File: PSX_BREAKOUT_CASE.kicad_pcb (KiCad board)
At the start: 2 copper layers, 100 x 71.1 mm, 11 parts

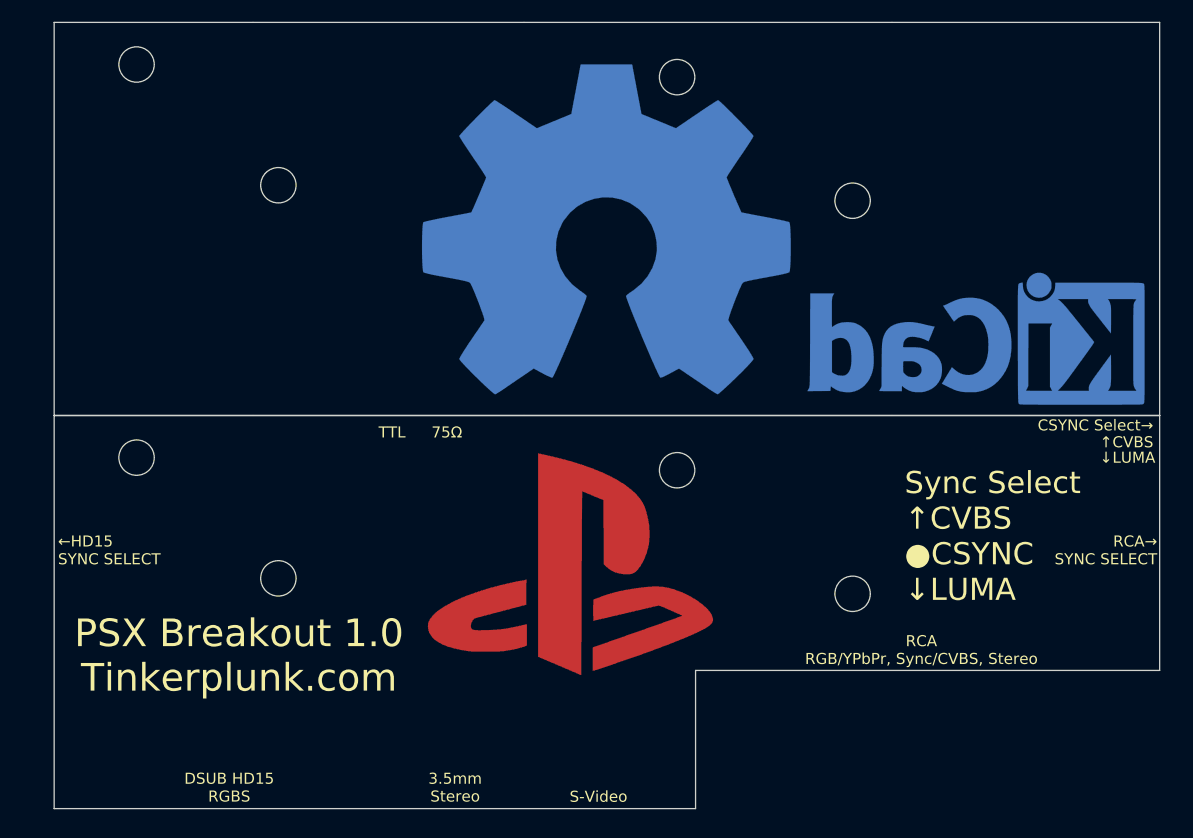
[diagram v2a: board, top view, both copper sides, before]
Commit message: Fixed s-video and headphone footprint, added support hole
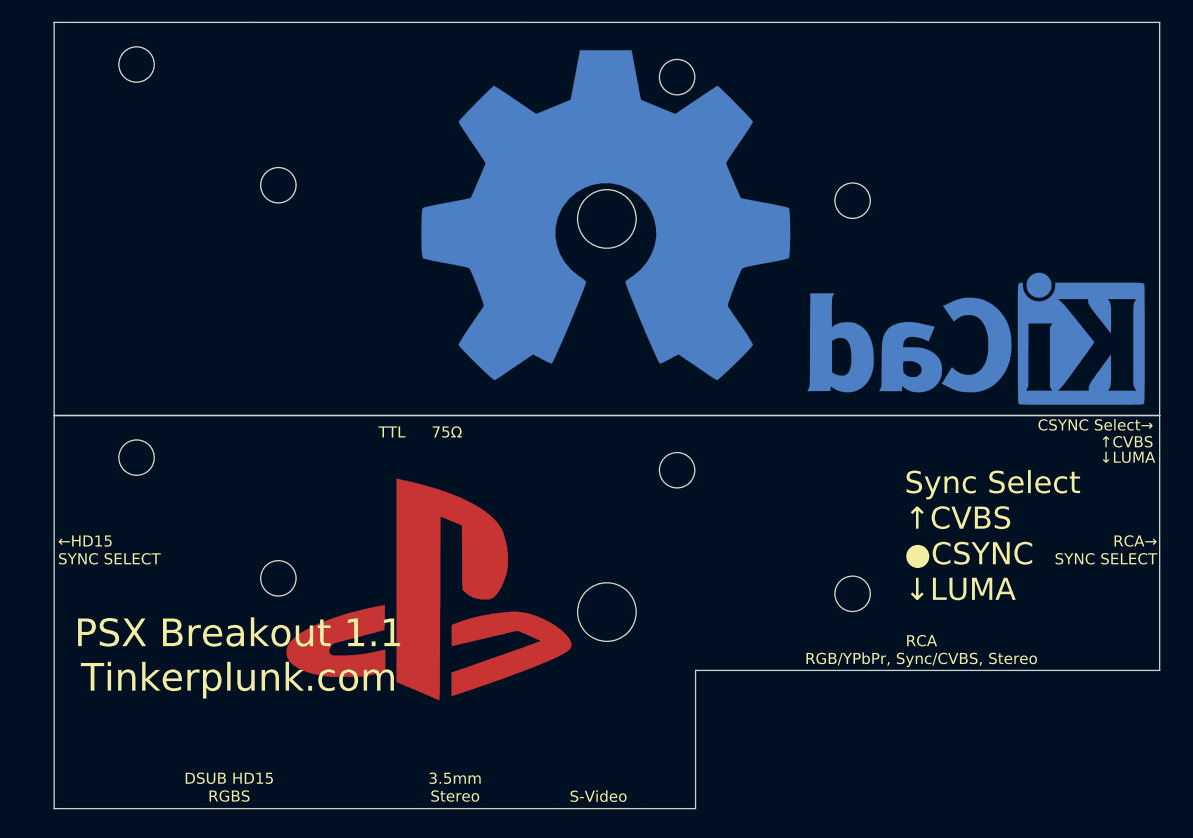
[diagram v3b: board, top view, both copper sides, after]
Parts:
- added REF**: MountingHole_5.3mm_M5, MountingHole:MountingHole_5.3mm_M5, F.Cu at (139.9, 58.4)
- added REF**: MountingHole_5.3mm_M5, MountingHole:MountingHole_5.3mm_M5, F.Cu at (140.0, 94.0)
- moved G*** 13.0 mm to (123.8, 92.0)
- moved REF** 1.29 mm to (139.9, 58.1)
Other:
- board text added: "PSX Breakout 1.1 Tinkerplunk.com"
- board text removed: "PSX Breakout 1.0 Tinkerplunk.com"
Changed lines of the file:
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@@
     (tracks 0)
     (zones 0)
-    (modules 11)
+    (modules 13)
     (nets 1)
   )
@@
     (uvia_drill 0.1)
   )
+  (module MountingHole:MountingHole_5.3mm_M5 (layer F.Cu)
+    (at 139.95 58.42)
+    (descr "Mounting Hole 5.3mm, no annular, M5")
+    (tags "mounting hole 5.3mm no annular m5")
+    (attr virtual)
+    (fp_text reference REF** (at 0 -6.3) (layer F.SilkS) hide
+      (effects (font (size 1 1) (thickness 0.15)))
+    )
+    (fp_text value MountingHole_5.3mm_M5 (at 0 6.3) (layer F.Fab)
+      (effects (font (size 1 1) (thickness 0.15)))
+    )
+    (fp_text user %R (at 0.3 0) (layer F.Fab)
+      (effects (font (size 1 1) (thickness 0.15)))
+    )
+    (fp_circle (center 0 0) (end 2.648001 0) (layer Cmts.User) (width 0.15))
+    (fp_circle (center 0 0) (end 2.648001 0) (layer F.CrtYd) (width 0.05))
+    (pad 1 np_thru_hole circle (at 0 0) (size 5.3 5.3) (drill 5.3) (layers *.Cu *.Mask))
+  )
+  (module MountingHole:MountingHole_5.3mm_M5 (layer F.Cu)
+    (at 139.954 93.98)
+    (descr "Mounting Hole 5.3mm, no annular, M5")
+    (tags "mounting hole 5.3mm no annular m5")
+    (attr virtual)
+    (fp_text reference REF** (at 0 -6.3) (layer F.SilkS) hide
+      (effects (font (size 1 1) (thickness 0.15)))
+    )
+    (fp_text value MountingHole_5.3mm_M5 (at 0 6.3) (layer F.Fab)
+      (effects (font (size 1 1) (thickness 0.15)))
+    )
+    (fp_circle (center 0 0) (end 2.648001 0) (layer F.CrtYd) (width 0.05))
+    (fp_circle (center 0 0) (end 2.648001 0) (layer Cmts.User) (width 0.15))
+    (fp_text user %R (at 0.3 0) (layer F.Fab)
+      (effects (font (size 1 1) (thickness 0.15)))
+    )
+    (pad 1 np_thru_hole circle (at 0 0) (size 5.3 5.3) (drill 5.3) (layers *.Cu *.Mask))
+  )
   (module MountingHole:MountingHole_3.2mm_M3 (layer F.Cu)
     (at 97.409 44.45)
@@
   )
   (module PSX_BREAKOUT:PSX_LOGO (layer F.Cu)
-    (at 136.652 89.662)
+    (at 123.85 91.95)
     (fp_text reference G*** (at 0 0) (layer F.SilkS) hide
       (effects (font (size 1.524 1.524) (thickness 0.3)))
@@
   )
   (module Symbol:OSHW-Symbol_33.5x30mm_Copper (layer B.Cu)
-    (at 139.954 59.436 180)
+    (at 139.9 58.15 180)
     (descr "Open Source Hardware Symbol")
     (tags "Logo Symbol OSHW")
@@
     (effects (font (size 2 2) (thickness 0.15)) (justify mirror))
   )
-  (gr_text "PSX Breakout 1.0\nTinkerplunk.com" (at 106.68 97.917) (layer F.SilkS)
+  (gr_text "PSX Breakout 1.1\nTinkerplunk.com" (at 106.68 97.917) (layer F.SilkS)
     (effects (font (size 2.5 2.5) (thickness 0.15)))
   )
